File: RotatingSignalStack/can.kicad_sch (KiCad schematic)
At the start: 3 parts, among them J1 Conn_01x02, U3 SN65HVD232

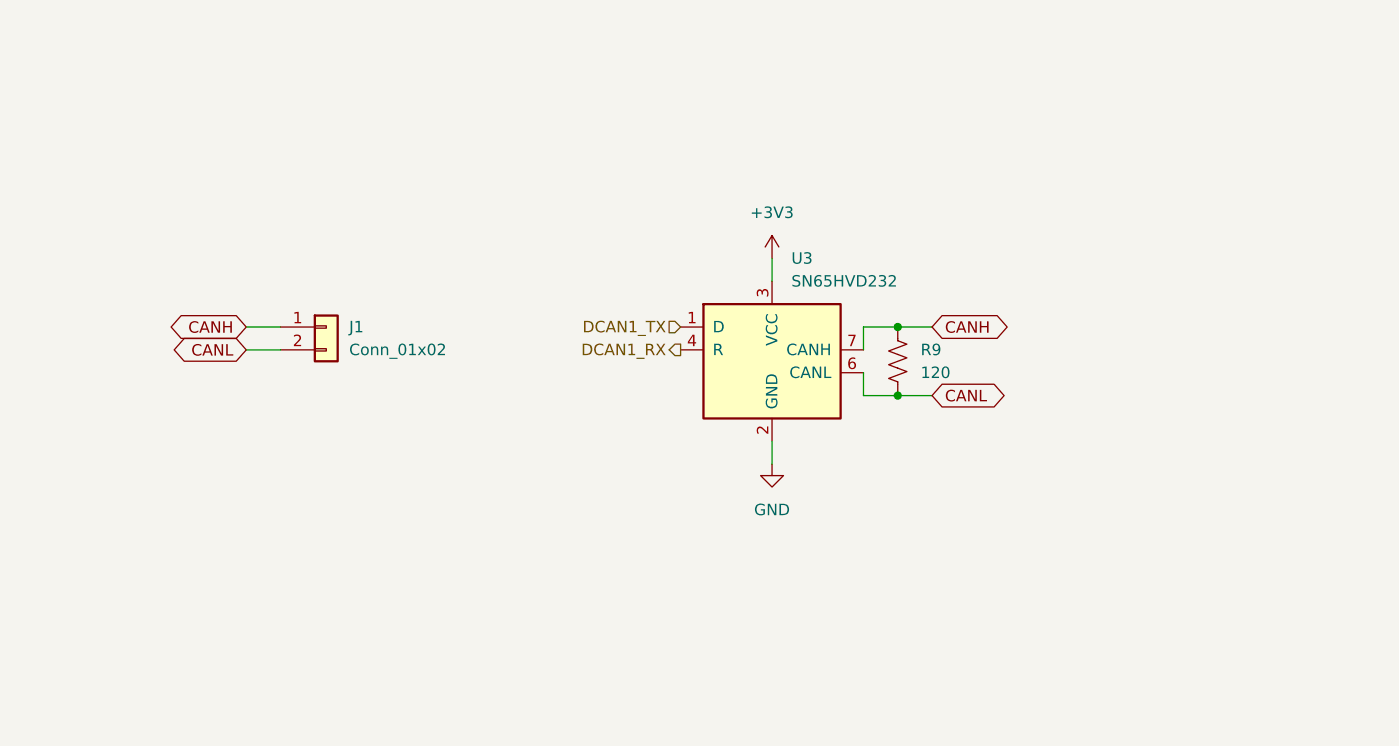
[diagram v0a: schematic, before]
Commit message: Added CAN ESD protection
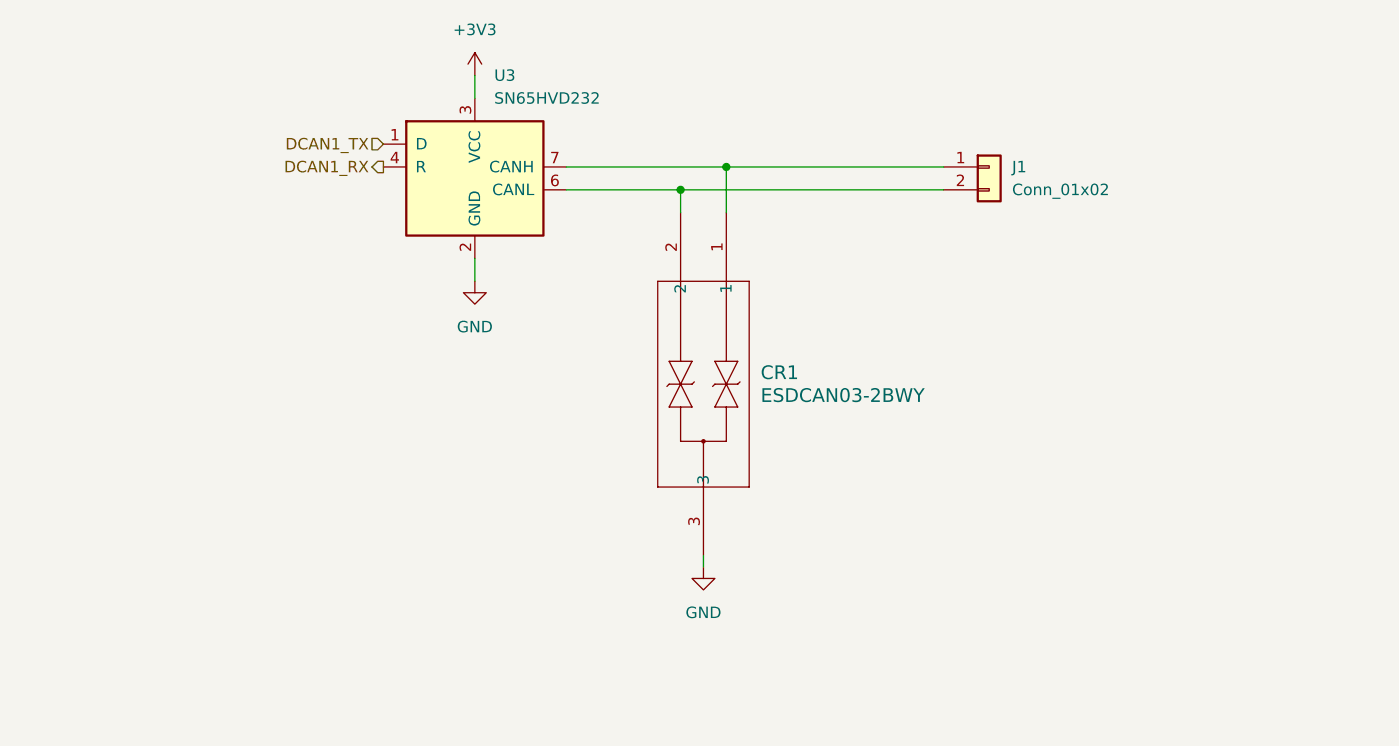
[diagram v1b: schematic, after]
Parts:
- removed R9: 120, symbol Device:R_US
- added CR1: ESDCAN03-2BWY, SOT323-3L_STM, symbol ESDCAN03-2BWY:ESDCAN03-2BWY
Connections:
- net GND: now also CR1.3
- net CANH: no longer names the net of J1.1 (Pin_1), U3.7 (CANH)
- net CANH: now also CR1.1
- net CANL: no longer names the net of J1.2 (Pin_2), U3.6 (CANL)
- net CANL: now also CR1.2
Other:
- moved on the sheet: J1, U3

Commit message: Added Motor connector CAN
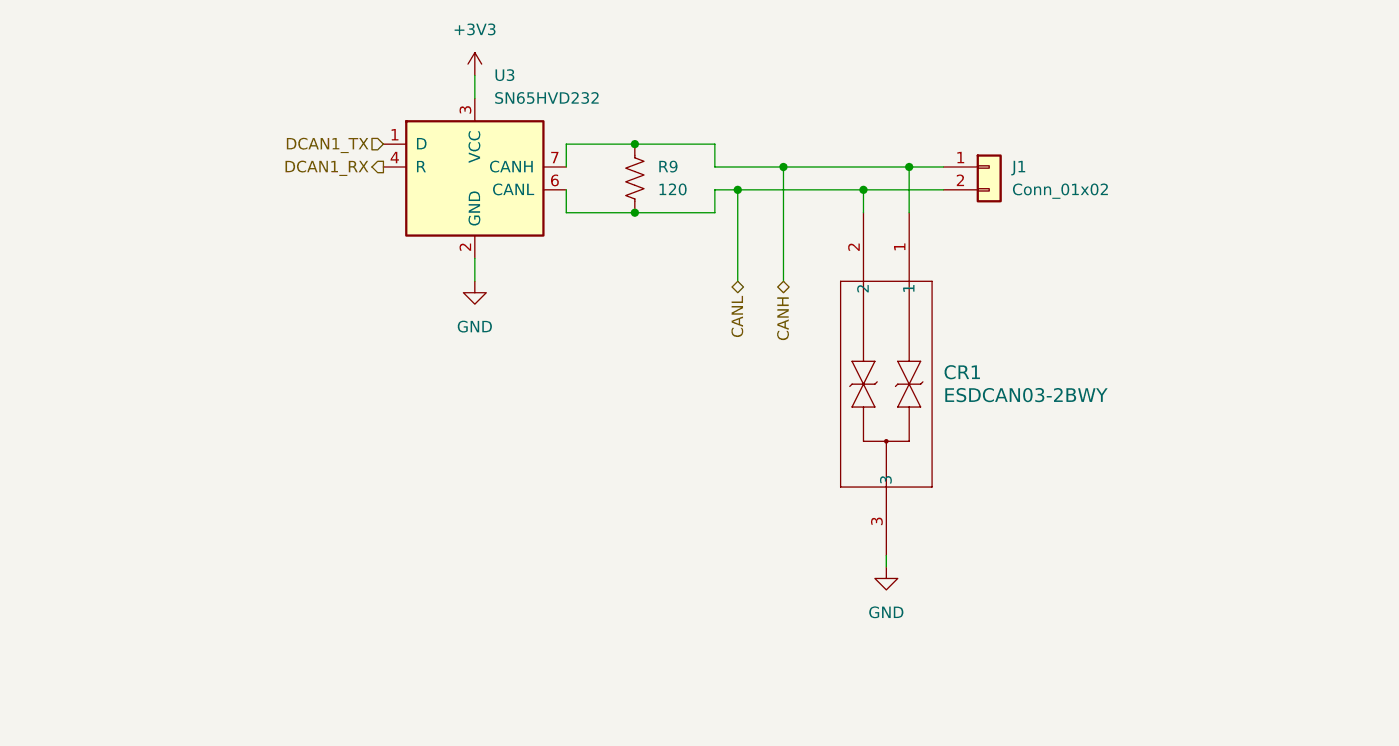
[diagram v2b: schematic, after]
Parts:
- added R9: 120, symbol Device:R_US
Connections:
- net CANL: now reaches CR1.2, J1.2 (Pin_2), U3.6 (CANL)
- net CANL: now also R9.2
- net CANH: now reaches CR1.1, J1.1 (Pin_1), U3.7 (CANH)
- net CANH: now also R9.1
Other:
- moved on the sheet: CR1

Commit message: Added everything
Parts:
- removed J1: Conn_01x02, Connector_JST:JST_SH_SM02B-SRSS-TB_1x02-1MP_P1.00mm_Horizontal, symbol Connector_Generic:Conn_01x02
- added Conn1: Molex_uF_D_02, MRDT_Connectors:MOLEX_SL_02_Vertical, symbol MRDT_Connectors:Molex_uF_D_02
- CR1: footprint SOT323-3L_STM -> SignalStack:SOT323-3L_STM-L
- R9: footprint (none) -> Resistor_SMD:R_0603_1608Metric_Pad0.98x0.95mm_HandSolder
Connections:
- net CANH: now also Conn1.1
- net CANL: now also Conn1.2
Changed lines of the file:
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@@
 			)
 		)
-		(property "Footprint" ""
+		(property "Footprint" "Resistor_SMD:R_0603_1608Metric_Pad0.98x0.95mm_HandSolder"
 			(at 143.256 77.724 90)
 			(effects
@@
 	)
 	(symbol
+		(lib_id "MRDT_Connectors:Molex_uF_D_02")
+		(at 181.61 80.01 0)
+		(unit 1)
+		(exclude_from_sim no)
+		(in_bom yes)
+		(on_board yes)
+		(dnp no)
+		(fields_autoplaced yes)
+		(property "Reference" "Conn1"
+			(at 185.42 76.1999 0)
+			(effects
+				(font
+					(size 1.524 1.524)
+				)
+				(justify left)
+			)
+		)
+		(property "Value" "Molex_uF_D_02"
+			(at 185.42 78.7399 0)
+			(effects
+				(font
+					(size 1.524 1.524)
+				)
+				(justify left)
+			)
+		)
+		(property "Footprint" "MRDT_Connectors:MOLEX_SL_02_Vertical"
+			(at 181.61 82.55 0)
+			(effects
+				(font
+					(size 1.524 1.524)
+				)
+				(hide yes)
+			)
+		)
+		(property "Datasheet" ""
+			(at 181.61 82.55 0)
+			(effects
+				(font
+					(size 1.524 1.524)
+				)
+				(hide yes)
+			)
+		)
+		(property "Description" ""
+			(at 181.61 80.01 0)
+			(effects
+				(font
+					(size 1.27 1.27)
+				)
+				(hide yes)
+			)
+		)
+		(pin "1"
+		)
+		(pin "2"
+		)
+		(instances
+			(project ""
+				(path "/fbbbfa89-3c28-4cf8-856b-66ca7308742c/cbabed27-8b23-4966-a034-4798ce513316"
+					(reference "Conn1")
+					(unit 1)
+				)
+			)
+		)
+	)
+	(symbol
 		(lib_id "power:+3V3")
 		(at 124.46 66.04 0)
@@
 	)
 	(symbol
-		(lib_id "Connector_Generic:Conn_01x02")
-		(at 181.61 76.2 0)
-		(unit 1)
-		(exclude_from_sim no)
-		(in_bom yes)
-		(on_board yes)
-		(dnp no)
-		(fields_autoplaced yes)
-		(property "Reference" "J1"
-			(at 184.15 76.1999 0)
-			(effects
-				(font
-					(size 1.27 1.27)
-				)
-				(justify left)
-			)
-		)
-		(property "Value" "Conn_01x02"
-			(at 184.15 78.7399 0)
-			(effects
-				(font
-					(size 1.27 1.27)
-				)
-				(justify left)
-			)
-		)
-		(property "Footprint" "Connector_JST:JST_SH_SM02B-SRSS-TB_1x02-1MP_P1.00mm_Horizontal"
-			(at 181.61 76.2 0)
-			(effects
-				(font
-					(size 1.27 1.27)
-				)
-				(hide yes)
-			)
-		)
-		(property "Datasheet" "~"
-			(at 181.61 76.2 0)
-			(effects
-				(font
-					(size 1.27 1.27)
-				)
-				(hide yes)
-			)
-		)
-		(property "Description" "Generic connector, single row, 01x02, script generated (kicad-library-utils/schlib/autogen/connector/)"
-			(at 181.61 76.2 0)
-			(effects
-				(font
-					(size 1.27 1.27)
-				)
-				(hide yes)
-			)
-		)
-		(pin "1"
-		)
-		(pin "2"
-		)
-		(instances
-			(project "RotatingSignalStack"
-				(path "/fbbbfa89-3c28-4cf8-856b-66ca7308742c/cbabed27-8b23-4966-a034-4798ce513316"
-					(reference "J1")
-					(unit 1)
-				)
-			)
-		)
-	)
-	(symbol
 		(lib_id "ESDCAN03-2BWY:ESDCAN03-2BWY")
 		(at 172.72 81.28 270)
@@
 			)
 		)
-		(property "Footprint" "SOT323-3L_STM"
+		(property "Footprint" "SignalStack:SOT323-3L_STM-L"
 			(at 172.72 81.28 0)
 			(effects

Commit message: placement fix
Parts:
- removed Conn1: Molex_uF_D_02, MRDT_Connectors:MOLEX_SL_02_Vertical, symbol MRDT_Connectors:Molex_uF_D_02
- added Conn1: Molex_SL_04, MRDT_Connectors:MOLEX_SL_04_Horizontal, symbol MRDT_Connectors:Molex_SL_04
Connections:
- net CANH: now also Conn1.4
- net CANL: now also Conn1.3
- net GND: now also Conn1.2
- new net VBUS: Conn1.1
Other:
- moved on the sheet: CR1, R9, U3

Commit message: more layout
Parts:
- Conn1: footprint MRDT_Connectors:MOLEX_SL_04_Horizontal -> MRDT_Connectors:MOLEX_SL_04_Vertical
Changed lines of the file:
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@@
 			)
 		)
-		(property "Footprint" "MRDT_Connectors:MOLEX_SL_04_Horizontal"
+		(property "Footprint" "MRDT_Connectors:MOLEX_SL_04_Vertical"
 			(at 204.47 92.71 0)
 			(effects
